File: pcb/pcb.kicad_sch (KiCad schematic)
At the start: 0 parts

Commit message: Add screw terminals and headers to schematic
The chosen power supply has two +V and -V output pairs, so we have two
screw terminals in parallel with the assumption that they have the same
voltage at all times. I put a 10uF cap between them to smooth out the DC
voltage and hopefully prevent transient spikes from the servos. I chose
10uF arbitrarily.

Each servo has its own 3-pin Dupont-style header to connect to for power
and control. This lets us place them anywhere on the board to make
hookup more convenient instead of a single long header.

The servo control signals from the microcontroller are routed to a
separate header. That header has extra pins routed to another empty
header in case we need extra sensors, like temperature sensors. With the
extra pins and header, we wouldn't need to order another board.
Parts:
- added C1: 10µF, symbol Device:C_Small_US
- added J1, J2, J3, J4: AMT0680001DB0000G, AMT0680001DB0000G, symbol AMT0680001DB0000G:AMT0680001DB0000G
- added J10: Conn_02x06_Counter_Clockwise, symbol Connector_Generic:Conn_02x06_Counter_Clockwise
- added J11: Conn_01x06, Connector:Tag-Connect_TC2030-IDC-NL_2x03_P1.27mm_Vertical, symbol Connector_Generic:Conn_01x06
- added J5, J6, J7, J8, J9: Conn_01x03, Connector:Tag-Connect_TC2030-IDC-NL_2x03_P1.27mm_Vertical, symbol Connector_Generic:Conn_01x03
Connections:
- new net: J10.10 (Pin_10), J11.3 (Pin_3)
- new net: J10.11 (Pin_11), J11.2 (Pin_2)
- new net: J10.12 (Pin_12), J11.1 (Pin_1)
- new net: J10.7 (Pin_7), J11.6 (Pin_6)
- new net: J10.8 (Pin_8), J11.5 (Pin_5)
- new net: J10.9 (Pin_9), J11.4 (Pin_4)
- new net +7V: C1.1, J1.1, J1.2, J1.3, J1.4, J1.5, J1.6, J2.1, J2.2, J2.3, J2.4, J2.5, J2.6, J5.2 (Pin_2), J6.2 (Pin_2), J7.2 (Pin_2), J8.2 (Pin_2), J9.2 (Pin_2)
- new net CTRL_ELBOW: J10.3 (Pin_3), J7.1 (Pin_1)
- new net CTRL_HAND: J10.5 (Pin_5), J9.1 (Pin_1)
- new net CTRL_HIP: J10.1 (Pin_1), J5.1 (Pin_1)
- new net CTRL_SHOULDER: J10.2 (Pin_2), J6.1 (Pin_1)
- new net CTRL_WRIST: J10.4 (Pin_4), J8.1 (Pin_1)
- new net GNDREF: C1.2, J10.6 (Pin_6), J3.1, J3.2, J3.3, J3.4, J3.5, J3.6, J4.1, J4.2, J4.3, J4.4, J4.5, J4.6, J5.3 (Pin_3), J6.3 (Pin_3), J7.3 (Pin_3), J8.3 (Pin_3), J9.3 (Pin_3)

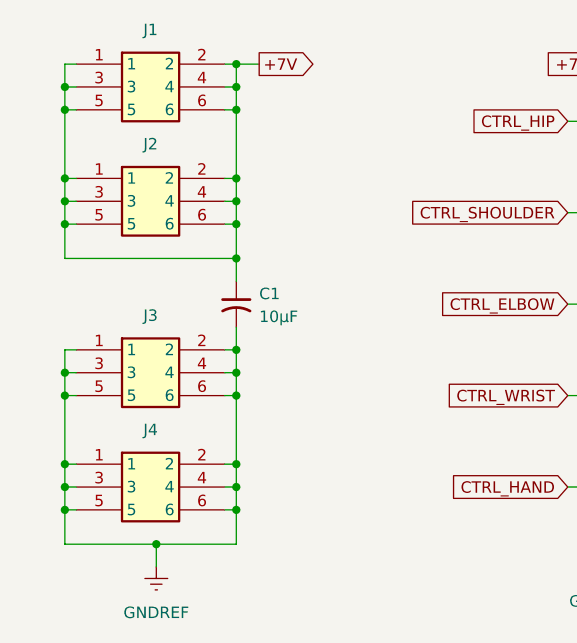
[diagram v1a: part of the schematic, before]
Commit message: Replace screw terminals with M4 screw connectors
We want to use the same ring connectors for both the power supply and
the PCB to reduce the number of components. The power supply we're using
has M3.5 screw connectors for its output. There weren't any M3.5 screw
connectors available for the PCB, so M4 was the next closest. We're
going to try using M4 connectors for both the PCB and the power supply
instead of the previous M8 screw connectors.
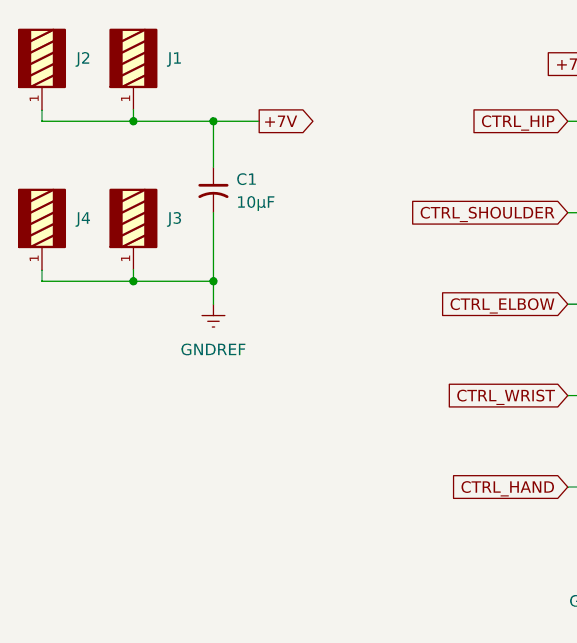
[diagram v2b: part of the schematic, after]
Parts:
- J1, J2, J3, J4: value AMT0680001DB0000G -> Screw Connector; footprint AMT0680001DB0000G -> WP-THRBU_THROUGH-HOLE:WP-THRBU_74650074; symbol AMT0680001DB0000G:AMT0680001DB0000G -> WP-THRBU_THROUGH-HOLE:WP-THRBU_THROUGH-HOLE; DATASHEET-URL (none) -> https://katalog.we-online.de/em/datasheet/74650074R.pdf; DigiKey Part Number 1818-AMT0680001DB0000G-ND -> 732-74650074RCT-ND; DigiKey URL https://www.digikey.com/en/products/detail/amphenol-anytek/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 -> https://www.digikey.com/en/products/detail/w%C3%BCrth-elekt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; IR (none) -> 50A; PART-NUMBER (none) -> 74650074R; PINS (none) -> 4; THREAD (none) -> M4
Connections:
- net +7V: no longer J1.2, J1.3, J1.4, J1.5, J1.6, J2.2, J2.3, J2.4, J2.5, J2.6
- net GNDREF: no longer J3.2, J3.3, J3.4, J3.5, J3.6, J4.2, J4.3, J4.4, J4.5, J4.6
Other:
- moved on the sheet: C1

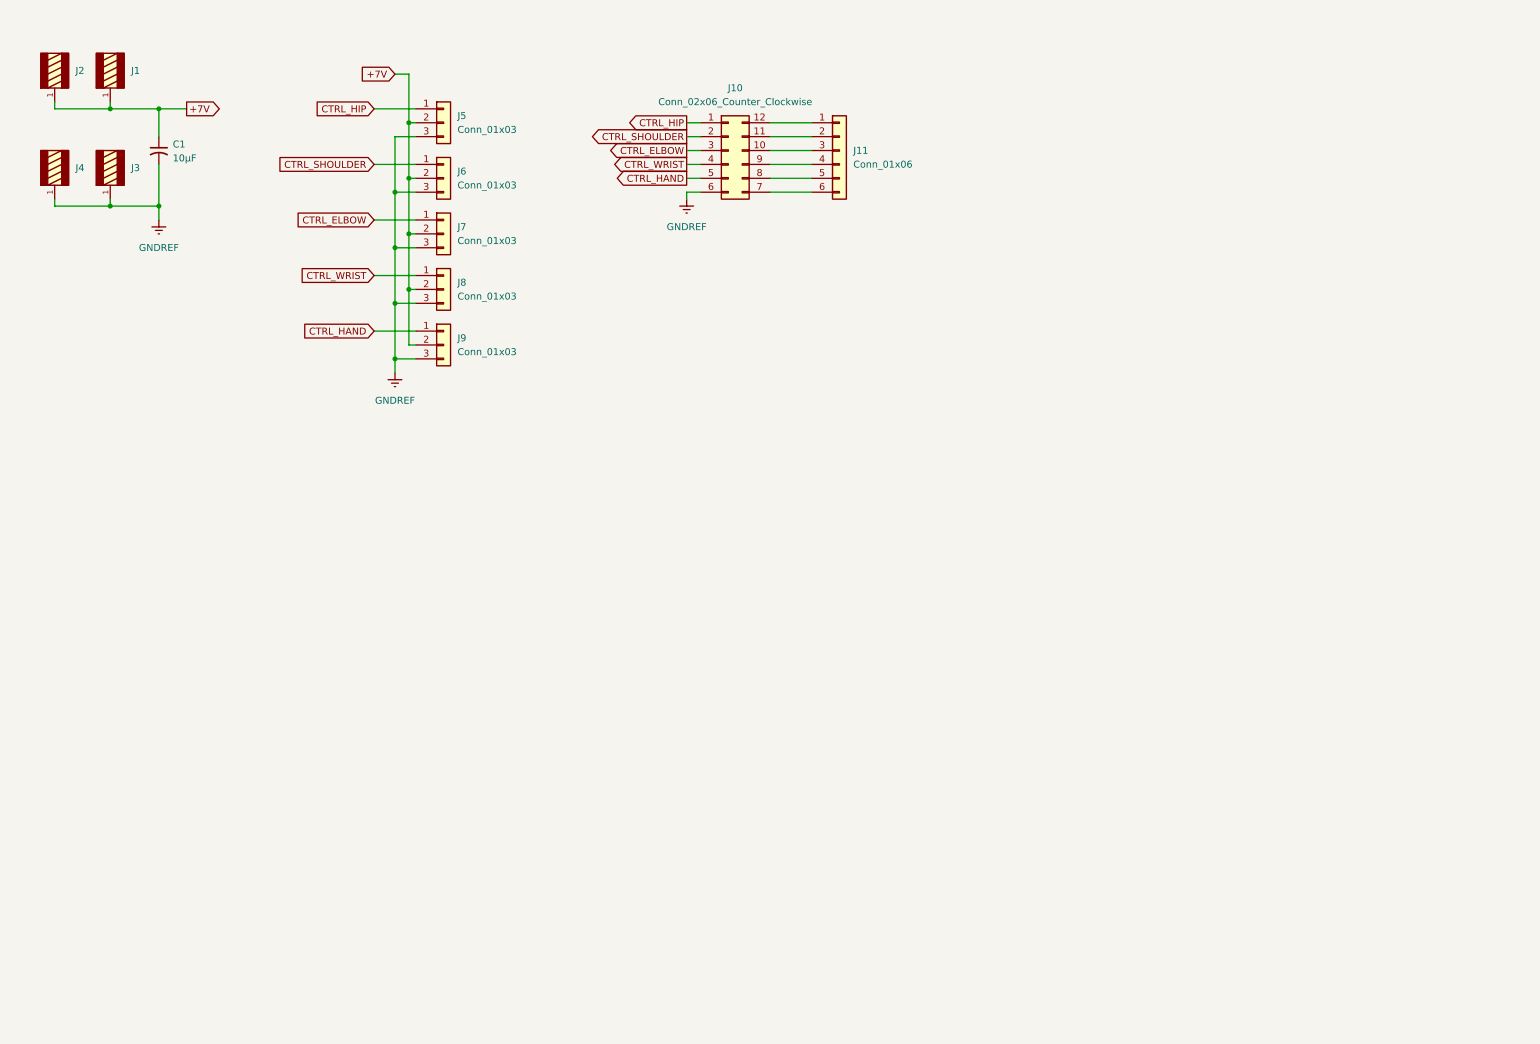
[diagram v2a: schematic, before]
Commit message: Add Hall effect sensors to schematic
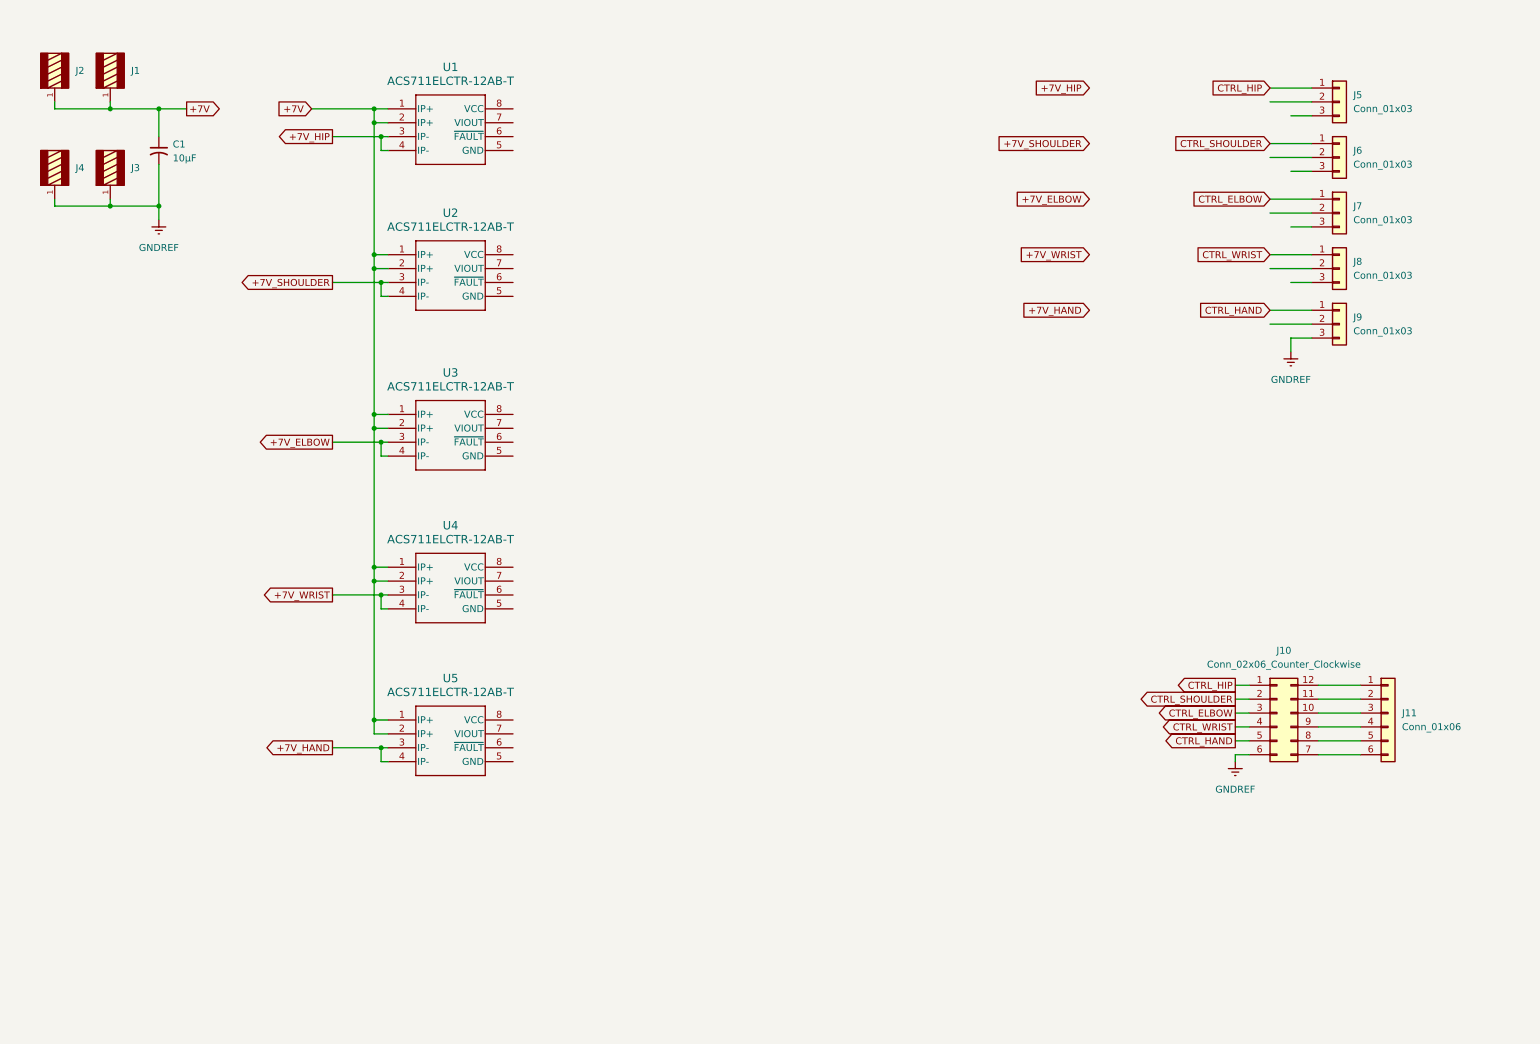
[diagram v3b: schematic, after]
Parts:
- added U1, U2, U3, U4, U5: ACS711ELCTR-12AB-T, SOICN-8_ALM, symbol ACS711ELCTR_12AB_T:ACS711ELCTR-12AB-T
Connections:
- net +7V: now also U1.1 (IP+), U1.2 (IP+), U2.1 (IP+), U2.2 (IP+), U3.1 (IP+), U3.2 (IP+), U4.1 (IP+), U4.2 (IP+), U5.1 (IP+), U5.2 (IP+); no longer J5.2 (Pin_2), J6.2 (Pin_2), J7.2 (Pin_2), J8.2 (Pin_2), J9.2 (Pin_2)
- net GNDREF: no longer J5.3 (Pin_3), J6.3 (Pin_3), J7.3 (Pin_3), J8.3 (Pin_3)
- new net +7V_ELBOW: U3.3 (IP-), U3.4 (IP-)
- new net +7V_HAND: U5.3 (IP-), U5.4 (IP-)
- new net +7V_HIP: U1.3 (IP-), U1.4 (IP-)
- new net +7V_SHOULDER: U2.3 (IP-), U2.4 (IP-)
- new net +7V_WRIST: U4.3 (IP-), U4.4 (IP-)
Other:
- moved on the sheet: J10, J11, J5, J6, J7, J8, J9

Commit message: Add overcurrent shutoff MOSFETs to schematic
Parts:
- removed J10: Conn_02x06_Counter_Clockwise, symbol Connector_Generic:Conn_02x06_Counter_Clockwise
- removed J11: Conn_01x06, Connector:Tag-Connect_TC2030-IDC-NL_2x03_P1.27mm_Vertical, symbol Connector_Generic:Conn_01x06
- added J10: Conn_02x10_Counter_Clockwise, symbol lib:Conn_02x10_Counter_Clockwise
- added J11: Conn_01x10, symbol lib:Conn_01x10
- added Q1, Q2, Q3, Q4, Q5: IRF9Z34NPBF, Package_TO_SOT_THT:TO-220-3_Vertical, symbol lib:IRF9Z34NPBF
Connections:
- net +7V_ELBOW: now also Q3.3 (S)
- net +7V_HAND: now also Q5.3 (S)
- net +7V_HIP: now also Q1.3 (S)
- net +7V_SHOULDER: now also Q2.3 (S)
- net +7V_WRIST: now also Q4.3 (S)
- net CTRL_ELBOW: now also J10.3 (Pin_3)
- net CTRL_HAND: now also J10.5 (Pin_5)
- net CTRL_HIP: now also J10.1 (Pin_1)
- net CTRL_SHOULDER: now also J10.2 (Pin_2)
- net CTRL_WRIST: now also J10.4 (Pin_4)
- net GNDREF: now also J5.3 (Pin_3), J6.3 (Pin_3), J7.3 (Pin_3), J8.3 (Pin_3), J10.11 (Pin_11)
- net at J7.2 (Pin_2): now also Q3.2 (D)
- net at J9.2 (Pin_2): now also Q5.2 (D)
- net at J5.2 (Pin_2): now also Q1.2 (D)
- net at J6.2 (Pin_2): now also Q2.2 (D)
- net at J8.2 (Pin_2): now also Q4.2 (D)
- new net: J10.12 (Pin_12), J11.9 (Pin_9)
- new net: J10.13 (Pin_13), J11.8 (Pin_8)
- new net: J10.14 (Pin_14), J11.7 (Pin_7)
- new net: J10.15 (Pin_15), J11.6 (Pin_6)
- new net: J10.16 (Pin_16), J11.5 (Pin_5)
- new net: J10.17 (Pin_17), J11.4 (Pin_4)
- new net: J10.18 (Pin_18), J11.3 (Pin_3)
- new net: J10.19 (Pin_19), J11.2 (Pin_2)
- new net: J10.20 (Pin_20), J11.1 (Pin_1)
- new net SHUTOFF_ELBOW: J10.8 (Pin_8), Q3.1 (G)
- new net SHUTOFF_HAND: J10.10 (Pin_10), Q5.1 (G)
- new net SHUTOFF_HIP: J10.6 (Pin_6), Q1.1 (G)
- new net SHUTOFF_SHOULDER: J10.7 (Pin_7), Q2.1 (G)
- new net SHUTOFF_WRIST: J10.9 (Pin_9), Q4.1 (G)
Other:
- moved on the sheet: J5, J6, J7, J8, J9

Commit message: Add passive comps and labels for HE sensors and level shifters
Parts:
- added C2, C3, C4, C5, C6: 100nF, symbol Device:C_Small
- added R1, R2, R3, R4, R5: 1k, symbol Device:R_Small_US
- added U6, U7, U8: TXS0102DCUR, TXS0102DCUR:SOP50P310X90-8N, symbol TXS0102DCUR:TXS0102DCUR
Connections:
- net GNDREF: now also U1.5 (GND), U2.5 (GND), U3.5 (GND), U4.5 (GND), U5.5 (GND), C2.2, C3.2, C4.2, C5.2, C6.2, U6.2 (GND), U7.2 (GND), U8.2 (GND)
- net at J10.12 (Pin_12): no longer J11.9 (Pin_9)
- net at J10.13 (Pin_13): no longer J11.8 (Pin_8)
- net at J10.14 (Pin_14): no longer J11.7 (Pin_7)
- net at J10.15 (Pin_15): no longer J11.6 (Pin_6)
- net at J11.5 (Pin_5): no longer J10.16 (Pin_16)
- net at J11.4 (Pin_4): no longer J10.17 (Pin_17)
- net at J11.3 (Pin_3): no longer J10.18 (Pin_18)
- net at J11.2 (Pin_2): no longer J10.19 (Pin_19)
- net at J11.1 (Pin_1): no longer J10.20 (Pin_20)
- net at U1.6 (~{FAULT}): now also R1.2
- net I_SENSE_HIP: now reaches U1.7 (VIOUT)
- net I_SENSE_HIP: now also J10.20 (Pin_20)
- net +3V3: now reaches U1.8 (VCC)
- net +3V3: now also U2.8 (VCC), U3.8 (VCC), U4.8 (VCC), U5.8 (VCC), C2.1, C3.1, C4.1, C5.1, C6.1, R1.1, R2.1, R3.1, R4.1, R5.1, U6.3 (V_{CCA}), U7.3 (V_{CCA}), U8.3 (V_{CCA})
- net at U5.6 (~{FAULT}): now also R5.2
- net I_SENSE_HAND: now reaches U5.7 (VIOUT)
- net I_SENSE_HAND: now also J10.16 (Pin_16)
- net at U2.6 (~{FAULT}): now also R2.2
- net I_SENSE_SHOULDER: now reaches U2.7 (VIOUT)
- net I_SENSE_SHOULDER: now also J10.19 (Pin_19)
- net at U4.6 (~{FAULT}): now also R4.2
- net I_SENSE_WRIST: now reaches U4.7 (VIOUT)
- net I_SENSE_WRIST: now also J10.17 (Pin_17)
- net at U3.6 (~{FAULT}): now also R3.2
- net I_SENSE_ELBOW: now reaches U3.7 (VIOUT)
- net I_SENSE_ELBOW: now also J10.18 (Pin_18)
- net SHUTOFF_ELBOW renamed SHUTOFF_ELBOW_H
- net SHUTOFF_ELBOW_H: now also U8.8 (B1); no longer J10.8 (Pin_8)
- net SHUTOFF_HAND renamed SHUTOFF_HAND_H
- net SHUTOFF_HAND_H: now also U7.1 (B2); no longer J10.10 (Pin_10)
- net SHUTOFF_HIP renamed SHUTOFF_HIP_H
- net SHUTOFF_HIP_H: now also U6.8 (B1); no longer J10.6 (Pin_6)
- net SHUTOFF_SHOULDER renamed SHUTOFF_SHOULDER_H
- net SHUTOFF_SHOULDER_H: now also U7.8 (B1); no longer J10.7 (Pin_7)
- net SHUTOFF_WRIST renamed SHUTOFF_WRIST_H
- net SHUTOFF_WRIST_H: now also U6.1 (B2); no longer J10.9 (Pin_9)
- new net +5V: U6.7 (V_{CCB}), U7.7 (V_{CCB}), U8.7 (V_{CCB})
- new net SHUTOFF_ELBOW_L: J10.8 (Pin_8), U8.5 (A1)
- new net SHUTOFF_HAND_L: J10.10 (Pin_10), U7.4 (A2)
- new net SHUTOFF_HIP_L: J10.6 (Pin_6), U6.5 (A1)
- new net SHUTOFF_SHOULDER_L: J10.7 (Pin_7), U7.5 (A1)
- new net SHUTOFF_WRIST_L: J10.9 (Pin_9), U6.4 (A2)
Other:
- moved on the sheet: J10, U1, U2, U3, U4, U5
